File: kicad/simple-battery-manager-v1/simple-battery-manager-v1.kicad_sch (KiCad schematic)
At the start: 14 parts, among them J1 BATT, J2 DC-INPUT, J2 OUTPUT, Q1 Si2301DS, Q2 Si2301DS

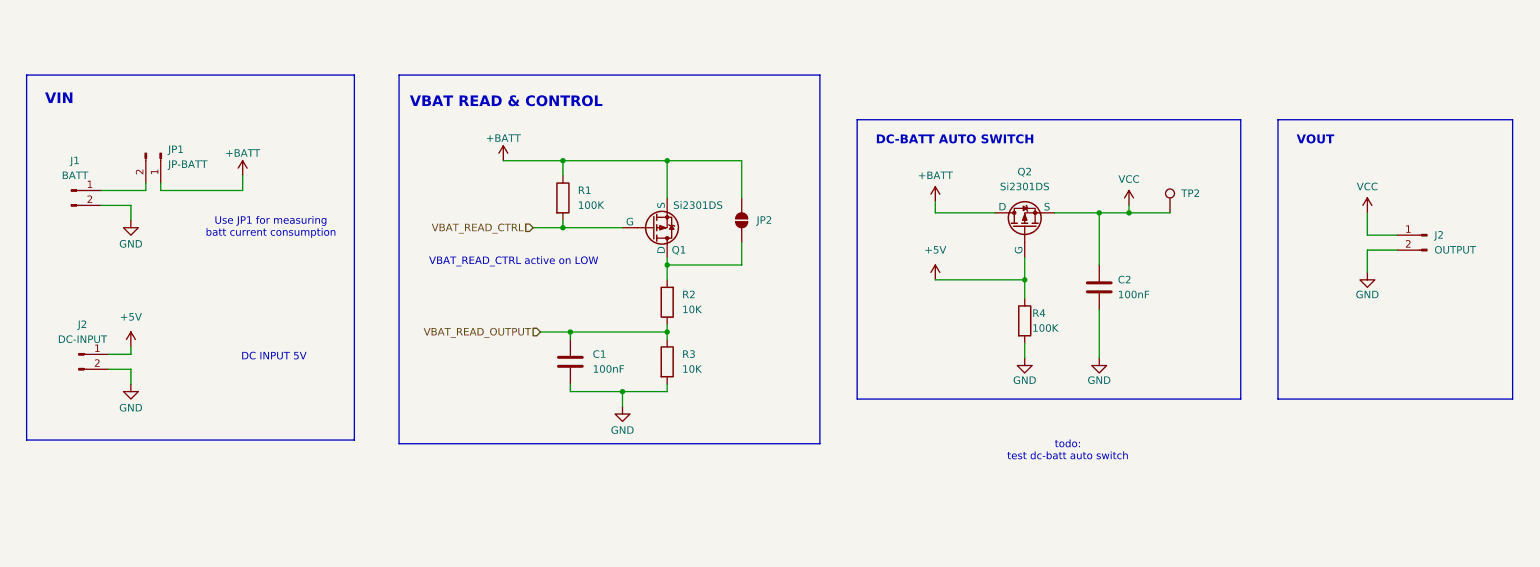
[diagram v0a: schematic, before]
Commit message: Updated autoswitch circuit, added D1. Added Headers for Vbat read and enable
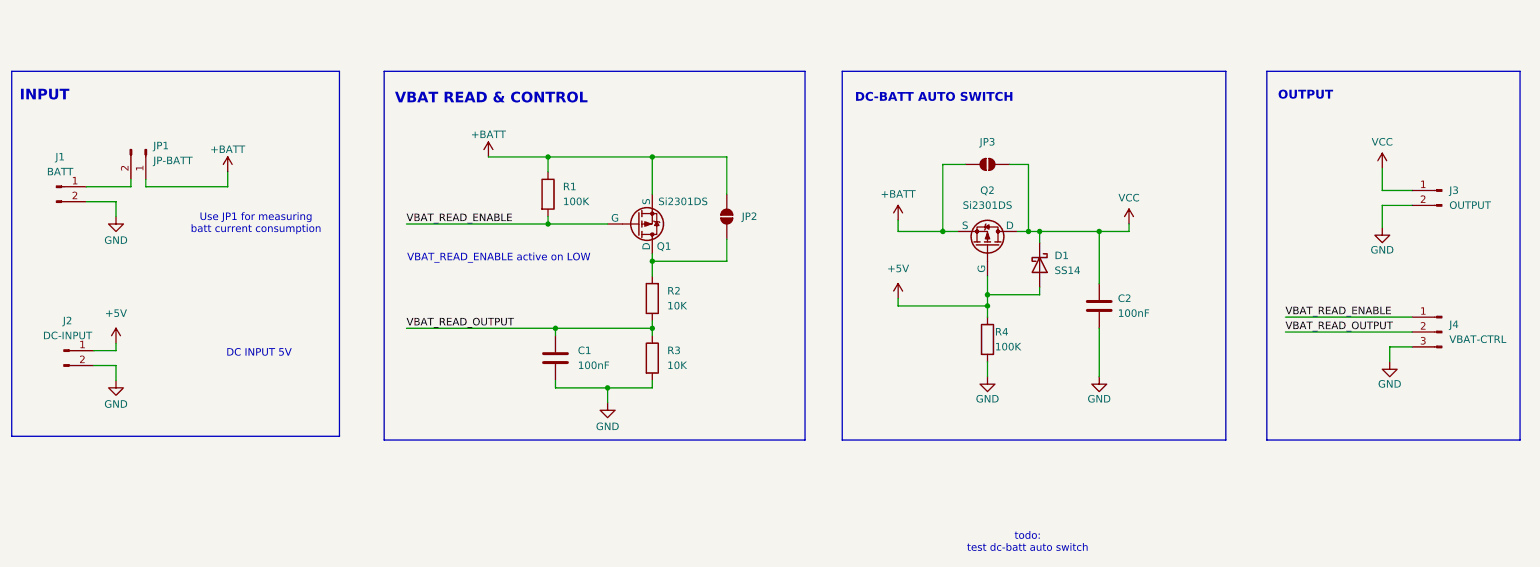
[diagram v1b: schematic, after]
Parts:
- removed TP2: TestPoint, TestPoint:TestPoint_Pad_D1.0mm, symbol Connector:TestPoint
- added D1: SS14, Diode_SMD:D_SMA, symbol Diode:SS14
- added J4: VBAT-CTRL, Connector_PinHeader_2.54mm:PinHeader_1x03_P2.54mm_Vertical, symbol Connector:Conn_01x03_Pin
- added JP3: SolderJumper_2_Open, Jumper:SolderJumper-2_P1.3mm_Open_TrianglePad1.0x1.5mm, symbol Jumper:SolderJumper_2_Open
- C1: footprint Capacitor_SMD:C_0603_1608Metric_Pad1.08x0.95mm_HandSolder -> Capacitor_SMD:C_0805_2012Metric_Pad1.18x1.45mm_HandSolder
- J1, J2, JP1: footprint (none) -> Connector_PinHeader_2.54mm:PinHeader_1x02_P2.54mm_Vertical
- J3: renamed from J2; footprint (none) -> Connector_PinHeader_2.54mm:PinHeader_1x02_P2.54mm_Vertical
- JP2: footprint (none) -> Jumper:SolderJumper-2_P1.3mm_Open_TrianglePad1.0x1.5mm
- R1, R2, R3: footprint Resistor_SMD:R_0603_1608Metric_Pad0.98x0.95mm_HandSolder -> Resistor_SMD:R_0805_2012Metric_Pad1.20x1.40mm_HandSolder
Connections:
- net +5V: now also D1.2 (A)
- net +BATT: now also Q2.3 (S), JP3.2 (B); no longer Q2.1 (D)
- net GND: now also J4.3 (Pin_3)
- net VBAT_READ_OUTPUT: now also J4.2 (Pin_2)
- net VCC: now also Q2.1 (D), D1.1 (K), JP3.1 (A); no longer Q2.3 (S)
- net VBAT_READ_CTRL renamed VBAT_READ_ENABLE
- net VBAT_READ_ENABLE: now also J4.1 (Pin_1)
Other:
- note added: "INPUT"
- note added: "OUTPUT"
- note added: "VBAT_READ_ENABLE active on LOW"
- note removed: "VBAT_READ_CTRL active on LOW"
- note removed: "VIN"
- note removed: "VOUT"
- moved on the sheet: C1, C2, J1, J2, J3, JP1, JP2, Q1, Q2, R1, R2, R3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

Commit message: Update footprints to 0603
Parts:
- C1, C2: footprint Capacitor_SMD:C_0805_2012Metric_Pad1.18x1.45mm_HandSolder -> Capacitor_SMD:C_0603_1608Metric_Pad1.08x0.95mm_HandSolder
- R1, R2, R3, R4: footprint Resistor_SMD:R_0805_2012Metric_Pad1.20x1.40mm_HandSolder -> Resistor_SMD:R_0603_1608Metric_Pad0.98x0.95mm_HandSolder
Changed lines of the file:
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@@
 			)
 		)
-		(property "Footprint" "Resistor_SMD:R_0805_2012Metric_Pad1.20x1.40mm_HandSolder"
+		(property "Footprint" "Resistor_SMD:R_0603_1608Metric_Pad0.98x0.95mm_HandSolder"
 			(at 183.642 119.38 90)
 			(effects
@@
 			)
 		)
-		(property "Footprint" "Capacitor_SMD:C_0805_2012Metric_Pad1.18x1.45mm_HandSolder"
+		(property "Footprint" "Capacitor_SMD:C_0603_1608Metric_Pad1.08x0.95mm_HandSolder"
 			(at 205.4352 117.475 0)
 			(effects
@@
 			)
 		)
-		(property "Footprint" "Capacitor_SMD:C_0805_2012Metric_Pad1.18x1.45mm_HandSolder"
+		(property "Footprint" "Capacitor_SMD:C_0603_1608Metric_Pad1.08x0.95mm_HandSolder"
 			(at 110.7948 118.745 0)
 			(effects
@@
 			)
 		)
-		(property "Footprint" "Resistor_SMD:R_0805_2012Metric_Pad1.20x1.40mm_HandSolder"
+		(property "Footprint" "Resistor_SMD:R_0603_1608Metric_Pad0.98x0.95mm_HandSolder"
 			(at 130.048 112.395 90)
 			(effects
@@
 			)
 		)
-		(property "Footprint" "Resistor_SMD:R_0805_2012Metric_Pad1.20x1.40mm_HandSolder"
+		(property "Footprint" "Resistor_SMD:R_0603_1608Metric_Pad0.98x0.95mm_HandSolder"
 			(at 108.712 94.615 90)
 			(effects
@@
 			)
 		)
-		(property "Footprint" "Resistor_SMD:R_0805_2012Metric_Pad1.20x1.40mm_HandSolder"
+		(property "Footprint" "Resistor_SMD:R_0603_1608Metric_Pad0.98x0.95mm_HandSolder"
 			(at 126.492 122.555 90)
 			(effects

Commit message: Sch finished.
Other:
- note removed: "todo: test dc-batt auto switch"
- moved on the sheet: C1, C2, D1, J1, J2, J3, J4, JP1, JP2, JP3, Q1, Q2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
